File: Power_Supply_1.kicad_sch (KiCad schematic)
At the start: 12 parts

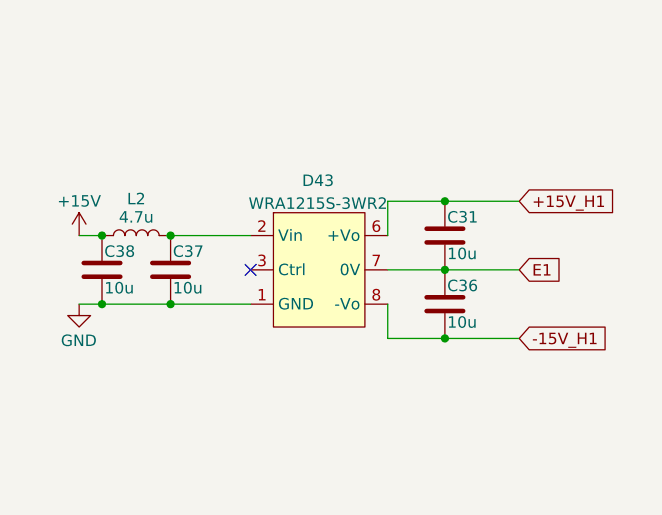
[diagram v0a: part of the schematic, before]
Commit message: VER2.2: начал менять источники питания драйверов
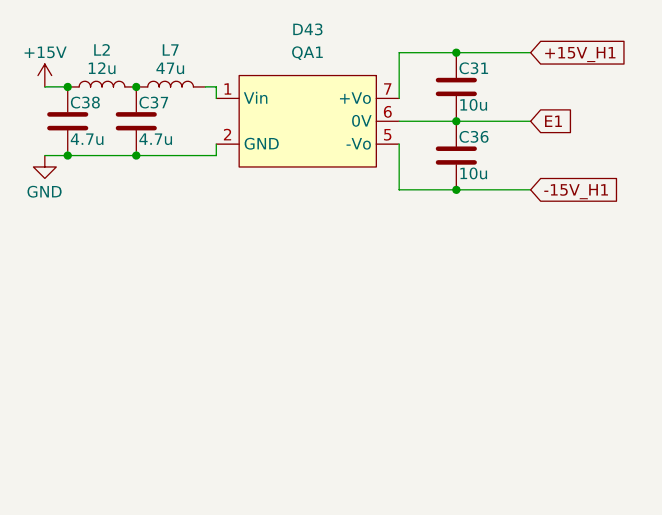
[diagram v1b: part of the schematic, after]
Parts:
- removed D43: WRA1215S-3WR2, Mornsun:WRA_S-3WR2, symbol Morsun:WRA1215S-3WR2
- added D43: QA1, DCDC_My:QA, symbol DCDC_My:QA1
- added L7: 47u, Inductor_SMD:L_1812_4532Metric_Pad1.30x3.40mm_HandSolder, symbol Device:L
- C37, C38: value 10u -> 4.7u; footprint Capacitor_SMD:C_1210_3225Metric_Pad1.33x2.70mm_HandSolder -> Capacitor_SMD:C_1206_3216Metric_Pad1.33x1.80mm_HandSolder
- L2: value 4.7u -> 12u; footprint Inductor_SMD:L_1812_4532Metric_Pad1.30x3.40mm_HandSolder -> Inductor_SMD:L_1210_3225Metric_Pad1.42x2.65mm_HandSolder
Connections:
- net +15V_H1: now also D43.7 (+Vo)
- net -15V_H1: now also D43.5 (-Vo)
- net E1: now also D43.6 (0V)
- net GND: now also D43.2 (GND)
- net at C37.1, L2.2: now also L7.1
- new net: D43.1 (Vin), L7.2
- no-connect marks 2 -> 1
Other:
- moved on the sheet: C31, C36, C37, C38, L2

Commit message: VER2.2: все изменения в списке изменений
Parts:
- removed D16: WRA1215S-3WR2, Mornsun:WRA_S-3WR2, symbol Morsun:WRA1215S-3WR2
- added D16: ~, DCDC_My:QA, symbol DCDC_My:QA1
- added L8: 47u, Inductor_SMD:L_1812_4532Metric_Pad1.30x3.40mm_HandSolder, symbol Device:L
- C4, C9: value 10u -> 4.7u; footprint Capacitor_SMD:C_1210_3225Metric_Pad1.33x2.70mm_HandSolder -> Capacitor_SMD:C_1206_3216Metric_Pad1.33x1.80mm_HandSolder
- D43: value QA1 -> ~; Description P/N (none) -> DCDC converter; Product Name (none) -> QA1
- L1: value 4.7u -> 12u; footprint Inductor_SMD:L_1812_4532Metric_Pad1.30x3.40mm_HandSolder -> Inductor_SMD:L_1210_3225Metric_Pad1.42x2.65mm_HandSolder; Product Name (none) -> LQH32MN120J23L
- L2: Product Name (none) -> LQH32MN120J23L
- L7: Product Name (none) -> LQH43CN470K03L
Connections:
- net +15V_L1: now also D16.7 (+Vo)
- net -15V_L1: now also D16.5 (-Vo)
- net E2: now also D16.6 (0V)
- net GND: now also D16.2 (GND)
- net at C9.1, L1.2: now also L8.1
- new net: D16.1 (Vin), L8.2
- no-connect marks 1 -> 0
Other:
- moved on the sheet: C10, C3, C4, C9, L1

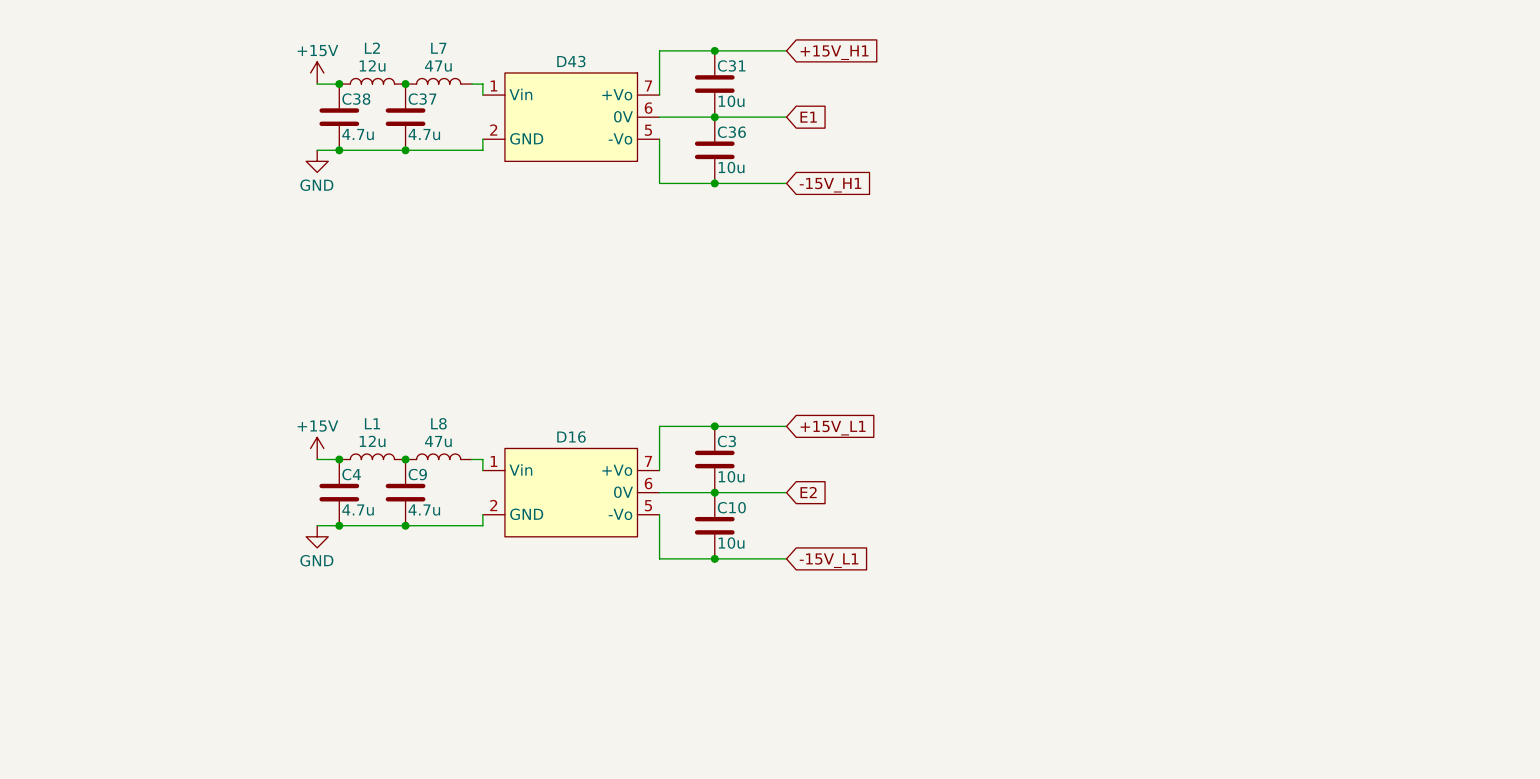
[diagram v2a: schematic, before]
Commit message: VER2.2: добавил фильтры на вход ШИМа и обновил все доки
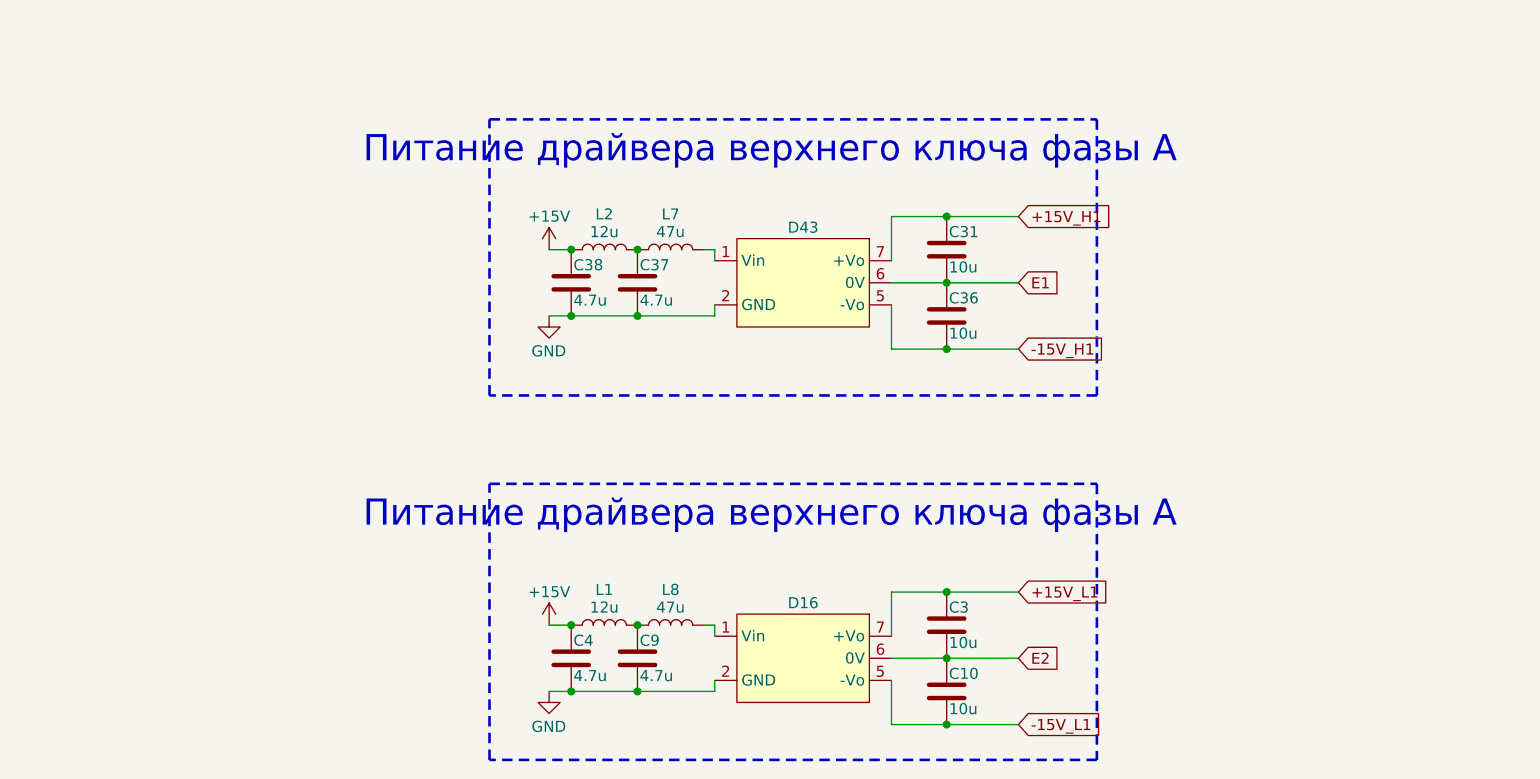
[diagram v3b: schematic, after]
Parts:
- L1, L2, L7, L8: Description P/N (none) -> Inductor SMD
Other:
- note added: "Питание драйвера верхнего ключа фазы А"
- company: (none) -> ООО "ЭТТ"
- moved on the sheet: C10, C3, C31, C36, C37, C38, C4, C9, D16, D43, L1, L2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

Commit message: VER2.2.1: создал папку для производственных доков
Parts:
- C10, C3, C31, C36: Description P/N (none) -> Capacitor SMD 50+V
- C37, C38, C4, C9: Description P/N (none) -> Capacitor SMD 25+V
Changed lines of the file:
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@@
 			)
 		)
-		(property "Description P/N" ""
+		(property "Description P/N" "Capacitor SMD 50+V"
 			(at 171.45 127 0)
 			(effects
@@
 			)
 		)
-		(property "Description P/N" ""
+		(property "Description P/N" "Capacitor SMD 50+V"
 			(at 171.45 91.44 0)
 			(effects
@@
 			)
 		)
-		(property "Description P/N" ""
+		(property "Description P/N" "Capacitor SMD 25+V"
 			(at 135.89 87.63 0)
 			(effects
@@
 			)
 		)
-		(property "Description P/N" ""
+		(property "Description P/N" "Capacitor SMD 25+V"
 			(at 128.27 130.81 0)
 			(effects
@@
 			)
 		)
-		(property "Description P/N" ""
+		(property "Description P/N" "Capacitor SMD 25+V"
 			(at 128.27 87.63 0)
 			(effects
@@
 			)
 		)
-		(property "Description P/N" ""
+		(property "Description P/N" "Capacitor SMD 25+V"
 			(at 135.89 130.81 0)
 			(effects
@@
 			)
 		)
-		(property "Description P/N" ""
+		(property "Description P/N" "Capacitor SMD 50+V"
 			(at 171.45 83.82 0)
 			(effects
@@
 			)
 		)
-		(property "Description P/N" ""
+		(property "Description P/N" "Capacitor SMD 50+V"
 			(at 171.45 134.62 0)
 			(effects

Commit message: VER2.2.1: исправил все доки
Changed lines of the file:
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@@
 		(date "2025-06-04")
 		(company "ООО \"ЭТТ\"")
+		(comment 1 "НВЦТ.EVP150-2-1.2000.120_v1 Э3")
 	)
 	(rectangle
@@
 					(size 1.27 1.27)
 				)
+				(hide yes)
 			)
 		)
@@
 					(size 1.27 1.27)
 				)
+				(hide yes)
 			)
 		)
@@
 					(size 1.27 1.27)
 				)
+				(hide yes)
 			)
 		)
@@
 					(size 1.27 1.27)
 				)
+				(hide yes)
 			)
 		)
@@
 					(size 1.27 1.27)
 				)
+				(hide yes)
 			)
 		)
@@
 					(size 1.27 1.27)
 				)
+				(hide yes)
 			)
 		)
@@
 					(size 1.27 1.27)
 				)
+				(hide yes)
 			)
 		)
@@
 					(size 1.27 1.27)
 				)
-			)
-		)
+				(hide yes)
+			)
+		)
